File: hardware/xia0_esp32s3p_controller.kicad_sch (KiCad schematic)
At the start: 5 parts, among them U2 XIAO-ESP32S3-PLUS

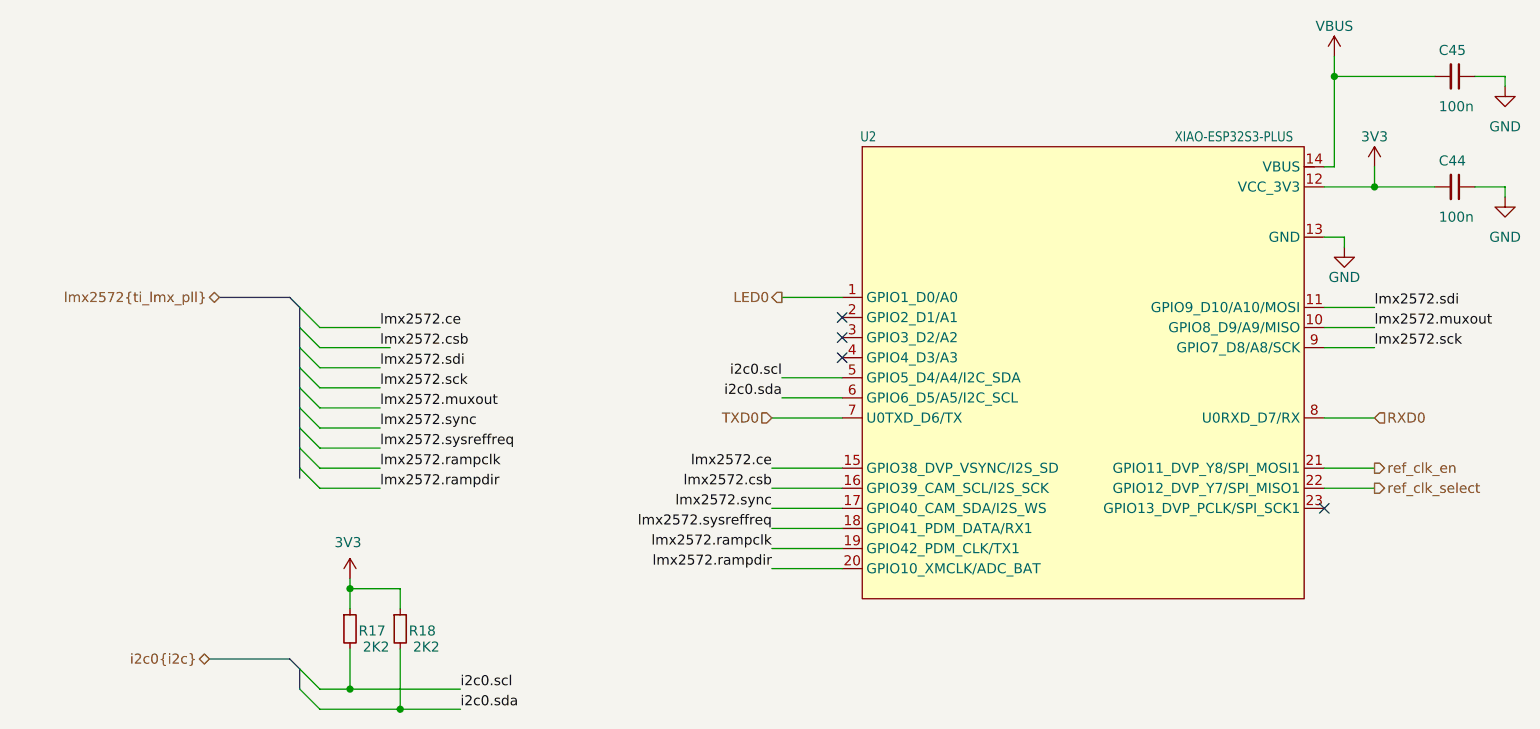
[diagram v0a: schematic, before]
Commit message: Completed core PCB routing
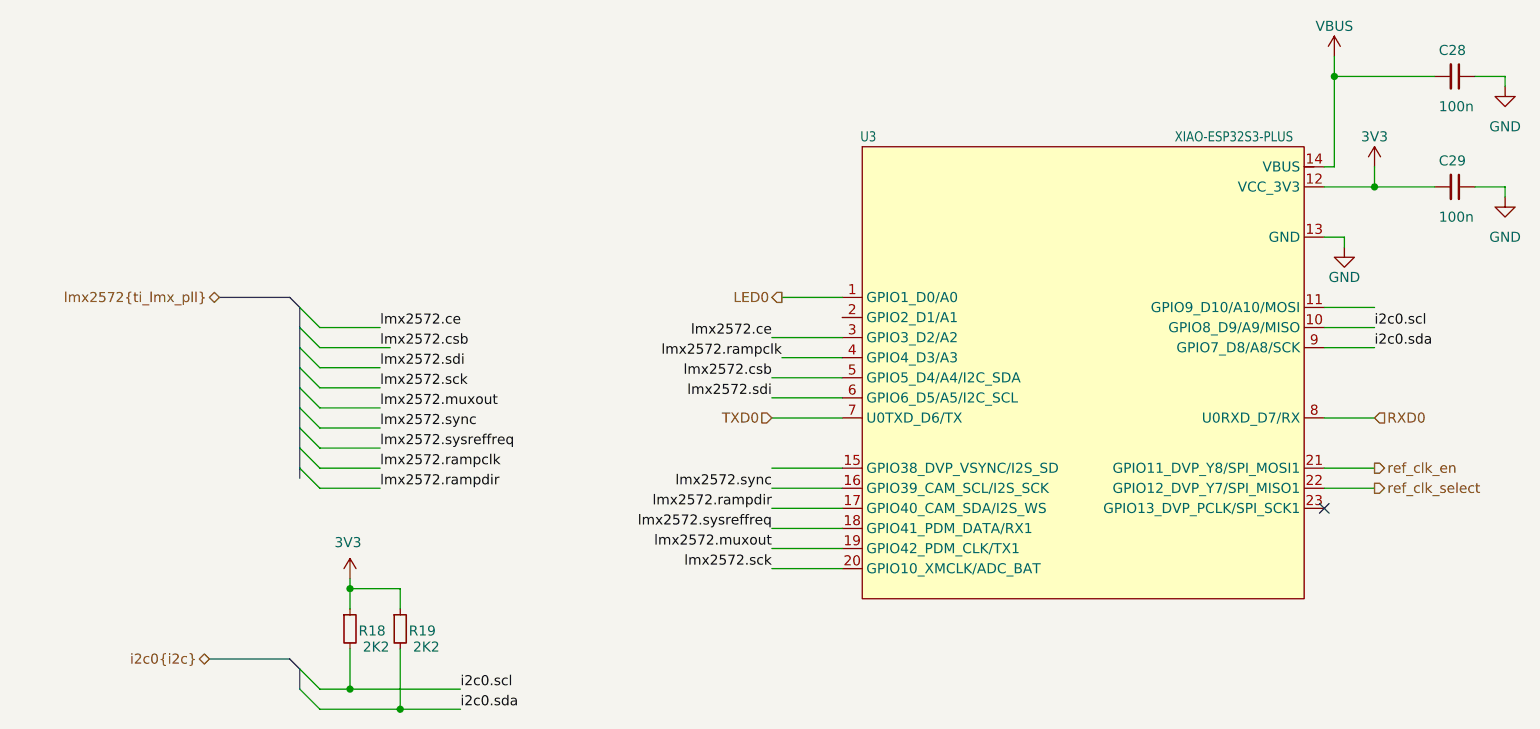
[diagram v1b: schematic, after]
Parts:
- renumbered C45 to C28, C44 to C29, R17 to R18, R18 to R19, U2 to U3
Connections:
- net i2c0.scl: now also U3.10 (GPIO8_D9/A9/MISO); no longer U3.5 (GPIO5_D4/A4/I2C_SDA)
- net i2c0.sda: now also U3.9 (GPIO7_D8/A8/SCK); no longer U3.6 (GPIO6_D5/A5/I2C_SCL)
- net lmx2572.ce: now also U3.3 (GPIO3_D2/A2); no longer U3.15 (GPIO38_DVP_VSYNC/I2S_SD)
- net lmx2572.csb: now also U3.5 (GPIO5_D4/A4/I2C_SDA); no longer U3.16 (GPIO39_CAM_SCL/I2S_SCK)
- net lmx2572.muxout: now also U3.19 (GPIO42_PDM_CLK/TX1); no longer U3.10 (GPIO8_D9/A9/MISO)
- net lmx2572.rampclk: now also U3.4 (GPIO4_D3/A3); no longer U3.19 (GPIO42_PDM_CLK/TX1)
- net lmx2572.rampdir: now also U3.17 (GPIO40_CAM_SDA/I2S_WS); no longer U3.20 (GPIO10_XMCLK/ADC_BAT)
- net lmx2572.sck: now also U3.20 (GPIO10_XMCLK/ADC_BAT); no longer U3.9 (GPIO7_D8/A8/SCK)
- net lmx2572.sdi: now also U3.6 (GPIO6_D5/A5/I2C_SCL); no longer U3.11 (GPIO9_D10/A10/MOSI)
- net lmx2572.sync: now also U3.16 (GPIO39_CAM_SCL/I2S_SCK); no longer U3.17 (GPIO40_CAM_SDA/I2S_WS)
- no-connect marks 4 -> 1
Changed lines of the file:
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@@
-	)
-	(no_connect
-		(at 121.92 93.98)
-	)
-	(no_connect
-		(at 121.92 88.9)
-	)
-	(no_connect
-		(at 121.92 91.44)
 	)
 	(no_connect
@@
 	(wire
 		(pts
+			(xy 113.03 91.44) (xy 121.92 91.44)
+		)
+		(stroke
+			(width 0)
+			(type default)
+		)
+	)
+	(wire
+		(pts
 			(xy 55.88 105.41) (xy 63.5 105.41)
 		)
@@
 	(wire
 		(pts
-			(xy 114.3 99.06) (xy 121.92 99.06)
+			(xy 113.03 99.06) (xy 121.92 99.06)
 		)
 		(stroke
@@
 		)
 	)
+	(wire
+		(pts
+			(xy 114.3 93.98) (xy 121.92 93.98)
+		)
+		(stroke
+			(width 0)
+			(type default)
+		)
+	)
 	(bus
 		(pts
@@
 	(wire
 		(pts
-			(xy 114.3 96.52) (xy 121.92 96.52)
+			(xy 113.03 96.52) (xy 121.92 96.52)
 		)
 		(stroke
@@
 	)
 	(label "lmx2572.ce"
-		(at 113.03 107.95 180)
+		(at 113.03 91.44 180)
 		(effects
 			(font
@@
 		)
 	)
+	(label "lmx2572.sync"
+		(at 113.03 110.49 180)
+		(effects
+			(font
+				(size 1.27 1.27)
+			)
+			(justify right bottom)
+		)
+	)
+	(label "lmx2572.sysreffreq"
+		(at 113.03 115.57 180)
+		(effects
+			(font
+				(size 1.27 1.27)
+			)
+			(justify right bottom)
+		)
+	)
+	(label "lmx2572.sdi"
+		(at 113.03 99.06 180)
+		(effects
+			(font
+				(size 1.27 1.27)
+			)
+			(justify right bottom)
+		)
+	)
 	(label "lmx2572.csb"
 		(at 63.5 92.71 0)
@@
 		)
 	)
-	(label "lmx2572.sck"
-		(at 189.23 92.71 0)
-		(effects
-			(font
-				(size 1.27 1.27)
-			)
-			(justify left bottom)
-		)
-	)
 	(label "lmx2572.rampclk"
 		(at 63.5 107.95 0)
@@
 		)
 	)
-	(label "i2c0.sda"
-		(at 114.3 99.06 180)
-		(effects
-			(font
-				(size 1.27 1.27)
-			)
-			(justify right bottom)
-		)
-	)
 	(label "lmx2572.sysreffreq"
 		(at 63.5 105.41 0)
@@
 		)
 	)
-	(label "lmx2572.csb"
-		(at 113.03 110.49 180)
+	(label "lmx2572.rampdir"
+		(at 113.03 113.03 180)
 		(effects
 			(font
@@
 		)
 	)
-	(label "lmx2572.rampdir"
-		(at 113.03 120.65 180)
-		(effects
-			(font
-				(size 1.27 1.27)
-			)
-			(justify right bottom)
-		)
-	)
-	(label "lmx2572.sdi"
-		(at 189.23 87.63 0)
+	(label "i2c0.scl"
+		(at 189.23 90.17 0)
 		(effects
 			(font
@@
 		)
 	)
-	(label "lmx2572.sync"
-		(at 113.03 113.03 180)
+	(label "lmx2572.sck"
+		(at 113.03 120.65 180)
 		(effects
 			(font
@@
 		)
 	)
-	(label "i2c0.scl"
-		(at 114.3 96.52 180)
+	(label "lmx2572.rampclk"
+		(at 114.3 93.98 180)
 		(effects
 			(font
@@
 			)
 			(justify right bottom)
-		)
-	)
-	(label "lmx2572.rampclk"
-		(at 113.03 118.11 180)
-		(effects
-			(font
-				(size 1.27 1.27)
-			)
-			(justify right bottom)
-		)
-	)
-	(label "lmx2572.muxout"
-		(at 189.23 90.17 0)
-		(effects
-			(font
-				(size 1.27 1.27)
-			)
-			(justify left bottom)
 		)
 	)
@@
 		)
 	)
-	(label "lmx2572.sysreffreq"
-		(at 113.03 115.57 180)
+	(label "lmx2572.csb"
+		(at 113.03 96.52 180)
 		(effects
 			(font
@@
 			)
 			(justify right bottom)
+		)
+	)
+	(label "lmx2572.muxout"
+		(at 113.03 118.11 180)
+		(effects
+			(font
+				(size 1.27 1.27)
+			)
+			(justify right bottom)
+		)
+	)
+	(label "i2c0.sda"
+		(at 189.23 92.71 0)
+		(effects
+			(font
+				(size 1.27 1.27)
+			)
+			(justify left bottom)
 		)
 	)
@@
 		(dnp no)
 		(fields_autoplaced yes)
-		(property "Reference" "#PWR09"
+		(property "Reference" "#PWR045"
 			(at 189.23 73.66 0)
 			(effects
@@
 			(project "radar-synth"
 				(path "/1b307ab8-316e-4a7c-b7a9-6aa9d087393d/3f4a7e3c-c9ad-4655-a24a-f1e04cc82a9b"
-					(reference "#PWR09")
+					(reference "#PWR045")
 					(unit 1)
 				)
@@
 		(on_board yes)
 		(dnp no)
-		(property "Reference" "R18"
+		(property "Reference" "R19"
 			(at 68.834 128.524 0)
 			(effects
@@
 			(project "radar-synth"
 				(path "/1b307ab8-316e-4a7c-b7a9-6aa9d087393d/3f4a7e3c-c9ad-4655-a24a-f1e04cc82a9b"
-					(reference "R18")
+					(reference "R19")
 					(unit 1)
 				)
@@
 		(on_board yes)
 		(dnp no)
-		(property "Reference" "#PWR029"
+		(property "Reference" "#PWR044"
 			(at 185.42 86.36 0)
 			(effects
@@
 			(project "radar-synth"
 				(path "/1b307ab8-316e-4a7c-b7a9-6aa9d087393d/3f4a7e3c-c9ad-4655-a24a-f1e04cc82a9b"
-					(reference "#PWR029")
+					(reference "#PWR044")
 					(unit 1)
 				)
@@
 		(on_board yes)
 		(dnp no)
-		(property "Reference" "C44"
+		(property "Reference" "C29"
 			(at 197.358 69.088 90)
 			(effects
@@
 			(project "radar-synth"
 				(path "/1b307ab8-316e-4a7c-b7a9-6aa9d087393d/3f4a7e3c-c9ad-4655-a24a-f1e04cc82a9b"
-					(reference "C44")
+					(reference "C29")
 					(unit 1)
 				)
@@
 		(on_board yes)
 		(dnp no)
-		(property "Reference" "R17"
+		(property "Reference" "R18"
 			(at 62.484 128.524 0)
 			(effects
@@
 			(project "radar-synth"
 				(path "/1b307ab8-316e-4a7c-b7a9-6aa9d087393d/3f4a7e3c-c9ad-4655-a24a-f1e04cc82a9b"
-					(reference "R17")
+					(reference "R18")
 					(unit 1)
 				)
@@
 		(dnp no)
 		(fields_autoplaced yes)
-		(property "Reference" "U2"
+		(property "Reference" "U3"
 			(at 125.222 66.04 0)
 			(do_not_autoplace yes)
@@
 			(project "radar-synth"
 				(path "/1b307ab8-316e-4a7c-b7a9-6aa9d087393d/3f4a7e3c-c9ad-4655-a24a-f1e04cc82a9b"
-					(reference "U2")
+					(reference "U3")
 					(unit 1)
 				)
@@
 		(dnp no)
 		(fields_autoplaced yes)
-		(property "Reference" "#PWR045"
+		(property "Reference" "#PWR046"
 			(at 205.74 66.04 0)
 			(effects
@@
 			(project "radar-synth"
 				(path "/1b307ab8-316e-4a7c-b7a9-6aa9d087393d/3f4a7e3c-c9ad-4655-a24a-f1e04cc82a9b"
-					(reference "#PWR045")
+					(reference "#PWR046")
 					(unit 1)
 				)
@@
 		(on_board yes)
 		(dnp no)
-		(property "Reference" "#PWR039"
+		(property "Reference" "#PWR042"
 			(at 59.69 125.73 0)
 			(effects
@@
 			(project "radar-synth"
 				(path "/1b307ab8-316e-4a7c-b7a9-6aa9d087393d/3f4a7e3c-c9ad-4655-a24a-f1e04cc82a9b"
-					(reference "#PWR039")
+					(reference "#PWR042")
 					(unit 1)
 				)
@@
 		(dnp no)
 		(fields_autoplaced yes)
-		(property "Reference" "#PWR044"
+		(property "Reference" "#PWR043"
 			(at 184.15 59.69 0)
 			(effects
@@
 			(project "radar-synth"
 				(path "/1b307ab8-316e-4a7c-b7a9-6aa9d087393d/3f4a7e3c-c9ad-4655-a24a-f1e04cc82a9b"
-					(reference "#PWR044")
+					(reference "#PWR043")
 					(unit 1)
 				)
@@
 		(dnp no)
 		(fields_autoplaced yes)
-		(property "Reference" "#PWR028"
+		(property "Reference" "#PWR047"
 			(at 205.74 80.01 0)
 			(effects
@@
 			(project "radar-synth"
 				(path "/1b307ab8-316e-4a7c-b7a9-6aa9d087393d/3f4a7e3c-c9ad-4655-a24a-f1e04cc82a9b"
-					(reference "#PWR028")
+					(reference "#PWR047")
 					(unit 1)
 				)
@@
 		(on_board yes)
 		(dnp no)
-		(property "Reference" "C45"
+		(property "Reference" "C28"
 			(at 197.358 55.118 90)
 			(effects
@@
 			(project "radar-synth"
 				(path "/1b307ab8-316e-4a7c-b7a9-6aa9d087393d/3f4a7e3c-c9ad-4655-a24a-f1e04cc82a9b"
-					(reference "C45")
+					(reference "C28")
 					(unit 1)
 				)

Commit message: Ready for FAB info
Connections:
- net i2c0.scl: now also U3.21 (GPIO11_DVP_Y8/SPI_MOSI1); no longer U3.10 (GPIO8_D9/A9/MISO)
- net i2c0.sda: now also U3.22 (GPIO12_DVP_Y7/SPI_MISO1); no longer U3.9 (GPIO7_D8/A8/SCK)
- net ref_clk_en: now also U3.9 (GPIO7_D8/A8/SCK); no longer U3.21 (GPIO11_DVP_Y8/SPI_MOSI1)
- net ref_clk_select: now also U3.10 (GPIO8_D9/A9/MISO); no longer U3.22 (GPIO12_DVP_Y7/SPI_MISO1)
- no-connect marks 1 -> 4
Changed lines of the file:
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@@
+	)
+	(no_connect
+		(at 182.88 87.63)
+	)
+	(no_connect
+		(at 121.92 107.95)
 	)
 	(no_connect
 		(at 182.88 113.03)
 	)
+	(no_connect
+		(at 121.92 88.9)
+	)
 	(bus_entry
 		(at 53.34 105.41)
@@
 	(wire
 		(pts
-			(xy 55.88 92.71) (xy 64.77 92.71)
+			(xy 55.88 92.71) (xy 63.5 92.71)
 		)
 		(stroke
@@
 	(wire
 		(pts
-			(xy 113.03 107.95) (xy 121.92 107.95)
-		)
-		(stroke
-			(width 0)
-			(type default)
-		)
-	)
-	(wire
-		(pts
 			(xy 59.69 123.19) (xy 59.69 125.73)
 		)
@@
 		(pts
 			(xy 59.69 130.81) (xy 59.69 135.89)
-		)
-		(stroke
-			(width 0)
-			(type default)
-		)
-	)
-	(wire
-		(pts
-			(xy 189.23 87.63) (xy 182.88 87.63)
 		)
 		(stroke
@@
 		)
 	)
-	(label "i2c0.scl"
-		(at 189.23 90.17 0)
+	(label "i2c0.sda"
+		(at 189.23 110.49 0)
 		(effects
 			(font
@@
 		)
 	)
+	(label "i2c0.scl"
+		(at 189.23 107.95 0)
+		(effects
+			(font
+				(size 1.27 1.27)
+			)
+			(justify left bottom)
+		)
+	)
 	(label "lmx2572.rampclk"
 		(at 114.3 93.98 180)
@@
 			)
 			(justify right bottom)
-		)
-	)
-	(label "i2c0.sda"
-		(at 189.23 92.71 0)
-		(effects
-			(font
-				(size 1.27 1.27)
-			)
-			(justify left bottom)
 		)
 	)
@@
 		)
 	)
-	(hierarchical_label "ref_clk_select"
-		(shape output)
-		(at 189.23 110.49 0)
-		(effects
-			(font
-				(size 1.27 1.27)
-			)
-			(justify left)
-		)
-	)
-	(hierarchical_label "ref_clk_en"
-		(shape output)
-		(at 189.23 107.95 0)
-		(effects
-			(font
-				(size 1.27 1.27)
-			)
-			(justify left)
-		)
-	)
 	(hierarchical_label "i2c0{i2c}"
 		(shape bidirectional)
@@
 		)
 	)
+	(hierarchical_label "ref_clk_en"
+		(shape output)
+		(at 189.23 92.71 0)
+		(effects
+			(font
+				(size 1.27 1.27)
+			)
+			(justify left)
+		)
+	)
+	(hierarchical_label "ref_clk_select"
+		(shape output)
+		(at 189.23 90.17 0)
+		(effects
+			(font
+				(size 1.27 1.27)
+			)
+			(justify left)
+		)
+	)
